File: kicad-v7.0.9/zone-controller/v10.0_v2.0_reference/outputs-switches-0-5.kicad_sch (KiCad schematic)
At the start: 84 parts, among them J1 EBBA-02-C-SS-BU, J2 EBBA-02-C-SS-BU, J3 EBBA-02-C-SS-BU, J4 EBBA-02-C-SS-BU, J5 EBBA-02-C-SS-BU, J6 EBBA-02-C-SS-BU, Q1 AOD458, Q16 2N7002A-YAN, Q2 AOD458, Q24 2N7002A-YAN, Q25 2N7002A-YAN, Q26 2N7002A-YAN, Q27 2N7002A-YAN, Q28 2N7002A-YAN, Q29 2N7002A-YAN, Q3 AOD458, Q30 2N7002A-YAN, Q31 2N7002A-YAN, Q32 2N7002A-YAN, Q33 2N7002A-YAN, Q34 2N7002A-YAN, Q4 AOD458, Q5 AOD458, Q6 AOD458, SW1 SMTS-102-2C2T, SW2 SMTS-102-2C2T, SW3 SMTS-102-2C2T, SW4 SMTS-102-2C2T, SW5 SMTS-102-2C2T, SW6 SMTS-102-2C2T

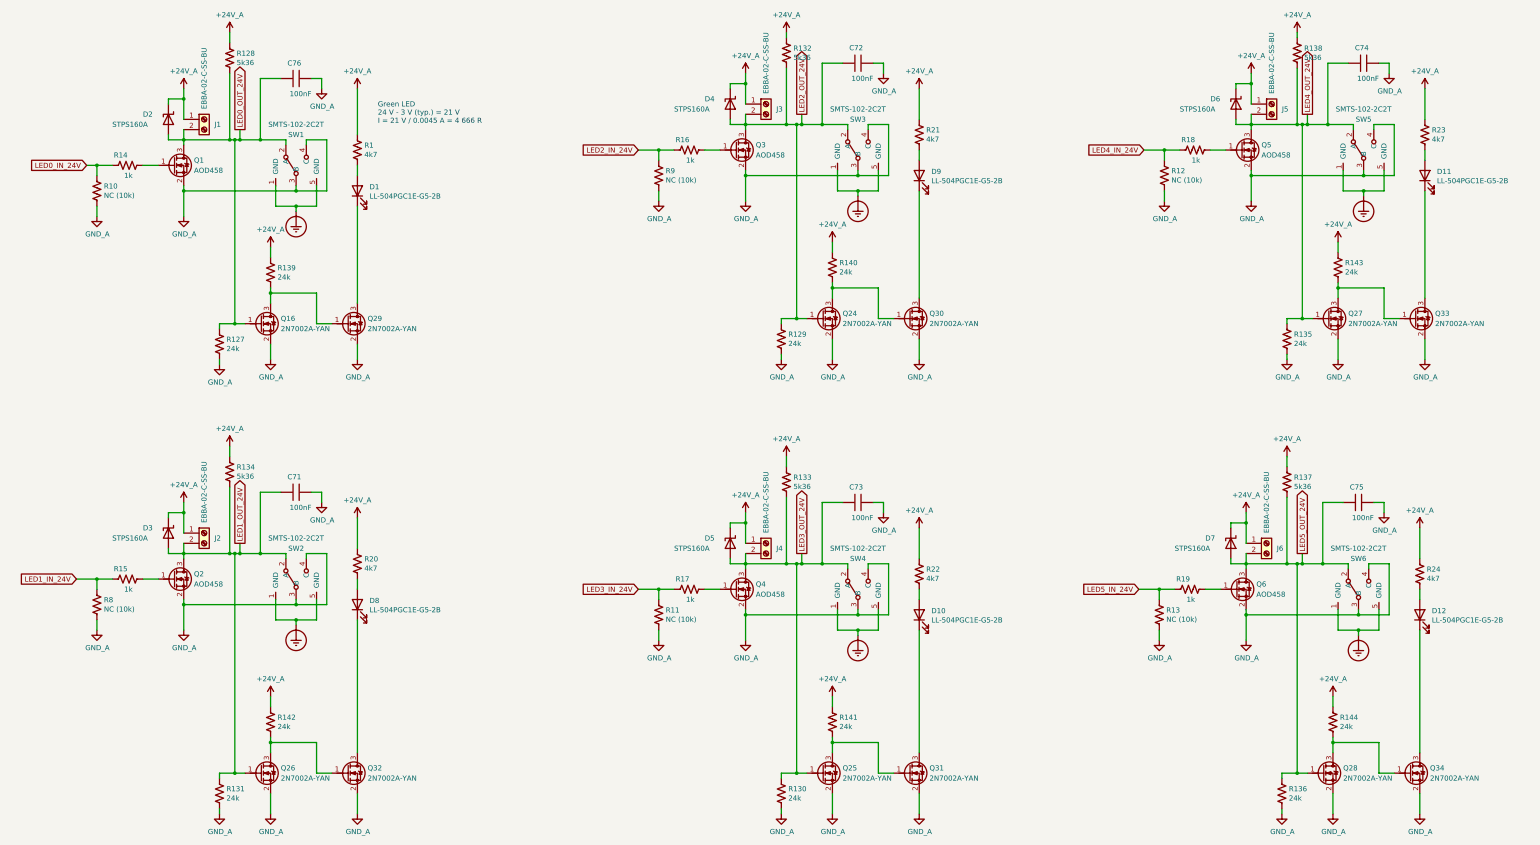
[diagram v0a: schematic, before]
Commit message: Zone controller. Change library. Small changes in schematic a PCB.
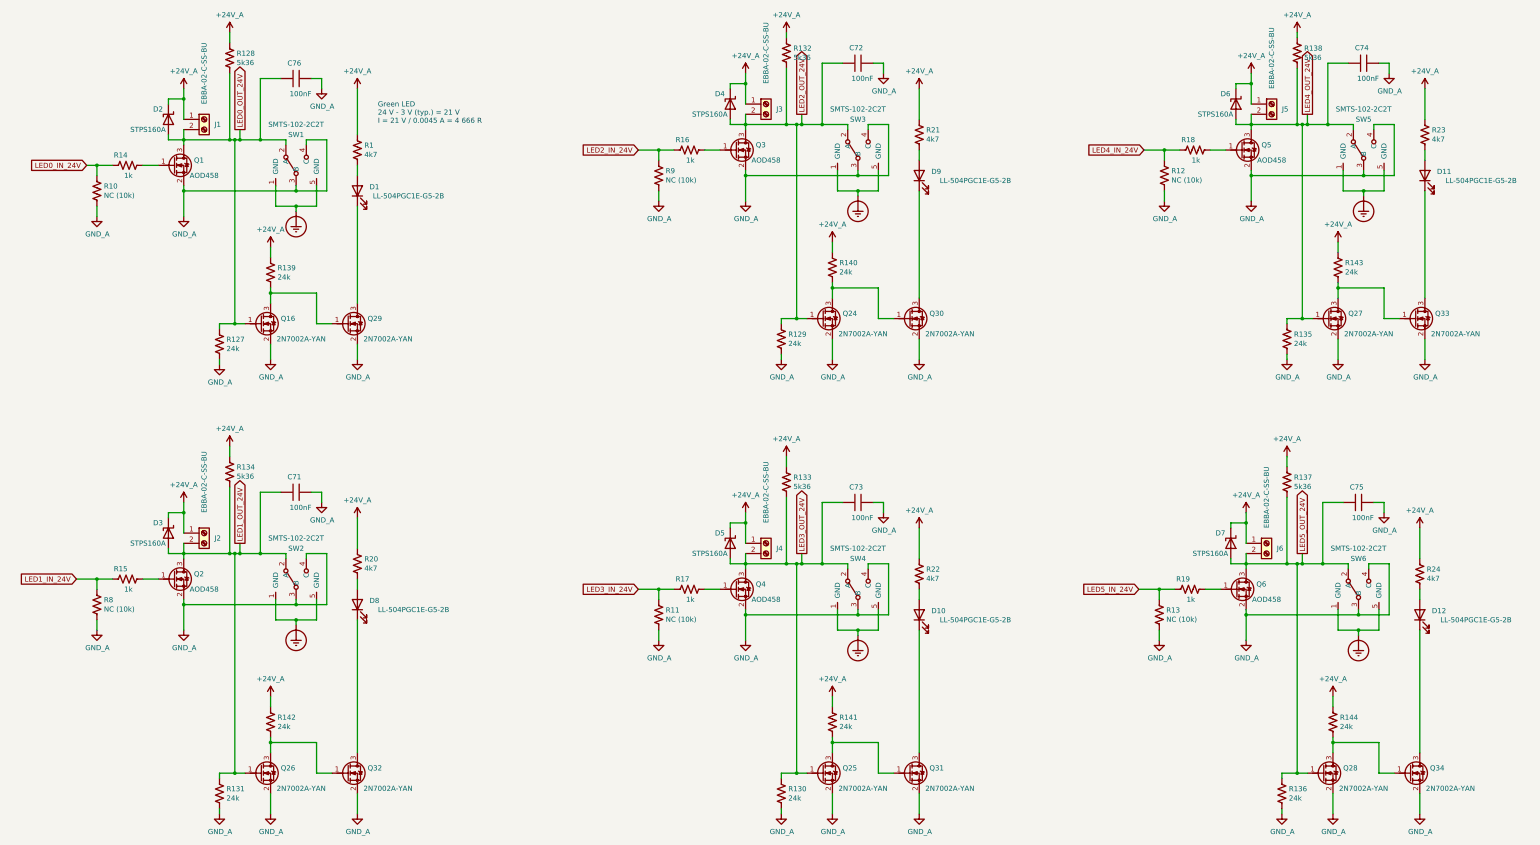
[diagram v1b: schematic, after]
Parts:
- C71, C72, C73, C74, C75, C76: symbol passive_component_rl:capacitor -> capacitor_smd_rl:c_1206
- D1, D10, D11, D12, D8, D9: symbol diode_rl:LED -> led_tht_rl:LL-504PGC1E-G5-2B
- D2, D3, D4, D5, D6, D7: symbol diode_rl:schottky_diode -> diode_smd_rl:STPS160A
- J1, J2, J3, J4, J5, J6: symbol connector_rl:1x2_screw_term_block -> terminal_block_tht_rl:EBBA-02-C-SS-BU
- Q1, Q2, Q3, Q4, Q5, Q6: symbol unipolar_transistor_rl:n_mosfet_gsd -> unipolar_transistor_smd_rl:AOD458
- Q16, Q24, Q25, Q26, Q27, Q28, Q29, Q30, Q31, Q32, Q33, Q34: symbol unipolar_transistor_rl:n_mosfet_gsd -> unipolar_transistor_smd_rl:2N7002A-YAN
- R1, R10, R11, R12, R127, R128, R129, R13, R130, R131, R132, R133, R134, R135, R136, R137, R138, R139, R14, R140, R141, R142, R143, R144, R15, R16, R17, R18, R19, R20, R21, R22, R23, R24, R8, R9: symbol passive_component_rl:resistor_us -> resistor_smd_rl:r_1206_us
- SW1, SW2, SW3, SW4, SW5, SW6: symbol switch_rl:SMTS-102-2C2T -> switch_tht_rl:SMTS-102-2C2T
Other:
- moved on the sheet: D2, D3, D4, D5, D6, D7
